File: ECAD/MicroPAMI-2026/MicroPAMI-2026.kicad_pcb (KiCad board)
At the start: 2 copper layers, 52 x 52 mm, 13 parts, among them J1 Conn_01x05, J2 Conn_01x05, SW3 SW_Push, U1 ATtiny3226-S, U2 ITR9608-F, U4 AMS1117-5.0, U5 ULN2803A

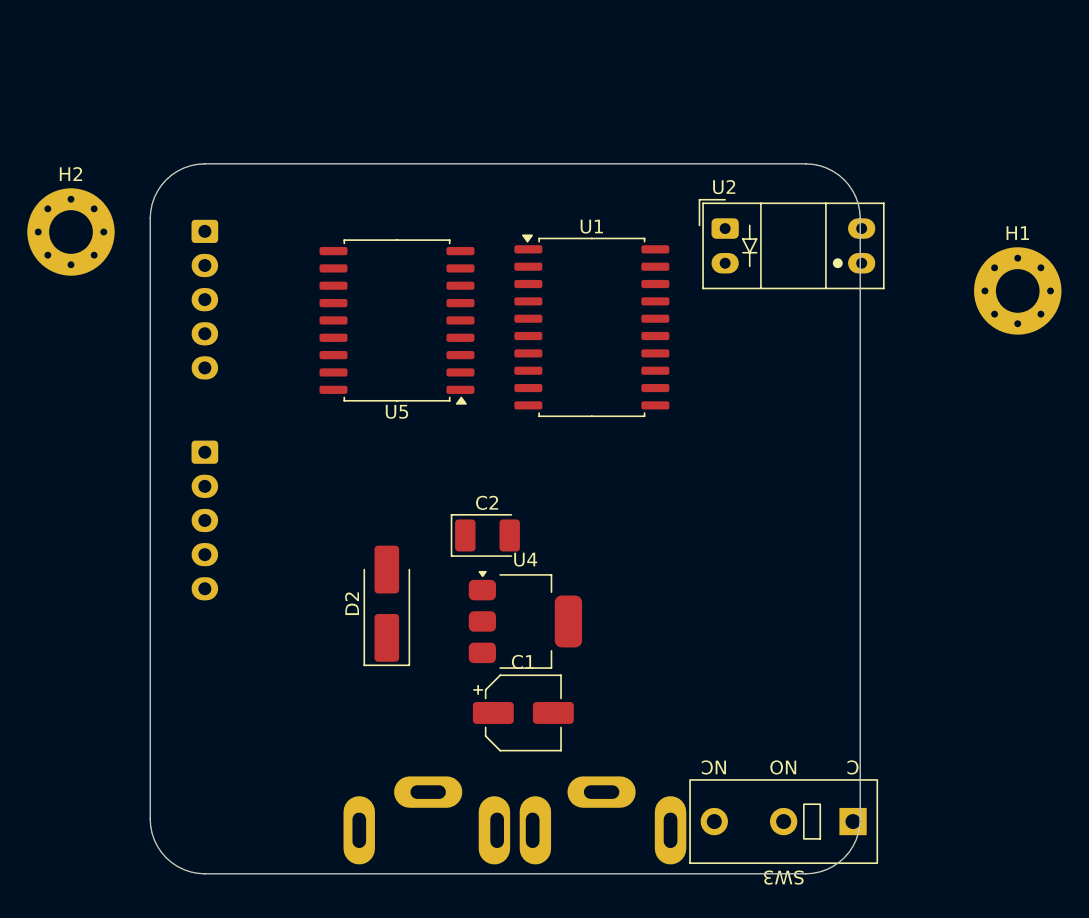
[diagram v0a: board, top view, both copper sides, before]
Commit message: Update PCB: add resistors, change net assignments
Added R3 and R8 SMD resistors to the PCB layout and updated net assignments for several signals, including connections for Tirette, LeftSensor, and others. Replaced unconnected net labels with specific net names for improved clarity. Updated backup files and made minor changes to project and cache files.
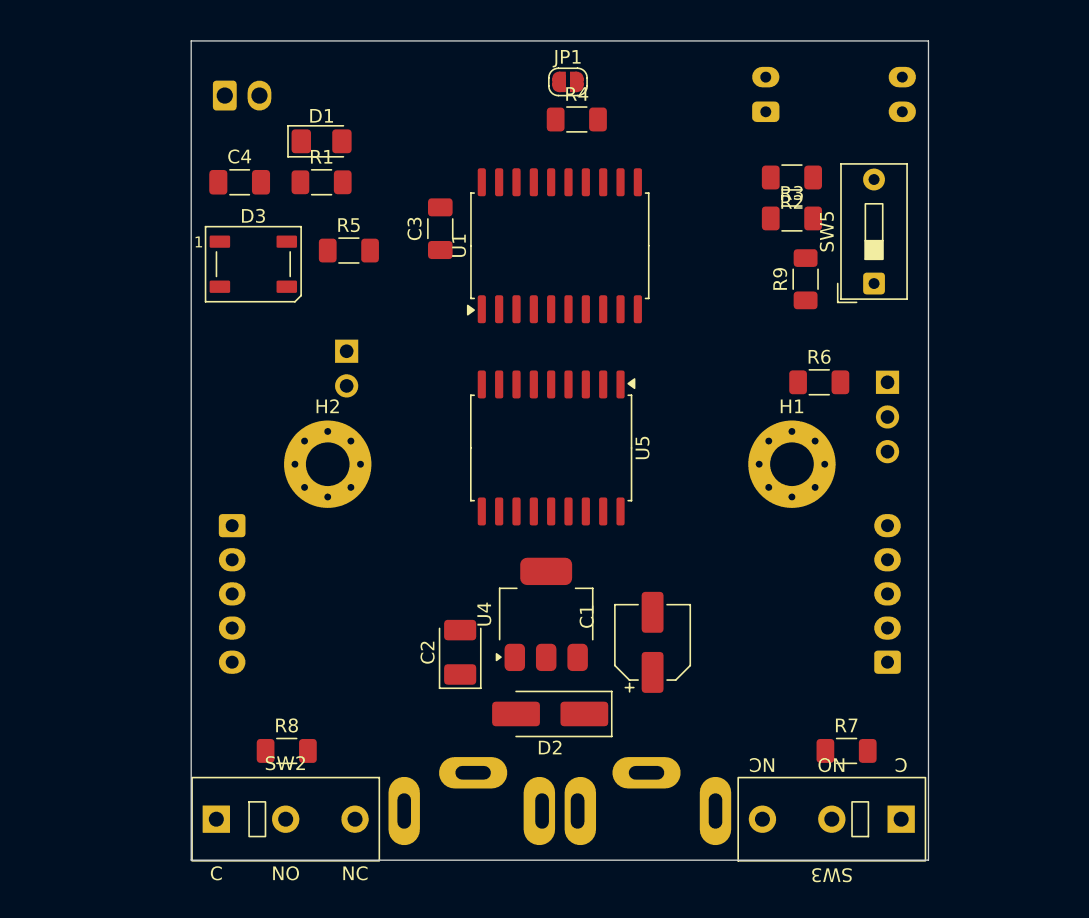
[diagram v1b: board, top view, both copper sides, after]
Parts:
- added C3: C_Small, Capacitor_SMD:C_1206_3216Metric_Pad1.33x1.80mm_HandSolder, F.Cu at (71.2, 70.8)
- added C4: C_Small, Capacitor_SMD:C_1206_3216Metric_Pad1.33x1.80mm_HandSolder, F.Cu at (56.5, 67.3)
- added D1: LED_Small, LED_SMD:LED_1206_3216Metric_Pad1.42x1.75mm_HandSolder, F.Cu at (62.5, 64.3)
- added D3: WS2812B, LED_SMD:LED_WS2812B_PLCC4_5.0x5.0mm_P3.2mm, F.Cu at (57.5, 73.3)
- added J3: MicroServo 2G, Connector_PinHeader_2.54mm:PinHeader_1x03_P2.54mm_Vertical, B.Cu at (104.0, 82.0)
- added J4: UPDI, Connector_PinHeader_2.54mm:PinHeader_1x02_P2.54mm_Horizontal, B.Cu at (64.4, 79.7)
- added JP1: Jumper_2_Small_Open, Jumper:SolderJumper-2_P1.3mm_Open_RoundedPad1.0x1.5mm, F.Cu at (80.6, 60.0)
- added R1: R_Small, Resistor_SMD:R_1206_3216Metric_Pad1.30x1.75mm_HandSolder, F.Cu at (62.5, 67.3)
- added R2: R_Small, Resistor_SMD:R_1206_3216Metric_Pad1.30x1.75mm_HandSolder, F.Cu at (97.0, 67.0)
- added R3: R_Small, Resistor_SMD:R_1206_3216Metric_Pad1.30x1.75mm_HandSolder, F.Cu at (97.0, 70.0)
- added R4: 4R7-470R, Resistor_SMD:R_1206_3216Metric_Pad1.30x1.75mm_HandSolder, F.Cu at (81.2, 62.8)
- added R5: 220, Resistor_SMD:R_1206_3216Metric_Pad1.30x1.75mm_HandSolder, F.Cu at (64.5, 72.3)
- added R6: 220, Resistor_SMD:R_1206_3216Metric_Pad1.30x1.75mm_HandSolder, F.Cu at (99.0, 82.0)
- added R7: 10k, Resistor_SMD:R_1206_3216Metric_Pad1.30x1.75mm_HandSolder, F.Cu at (101.0, 109.0)
- added R8: 10k, Resistor_SMD:R_1206_3216Metric_Pad1.30x1.75mm_HandSolder, F.Cu at (60.0, 109.0)
- added R9: 10k, Resistor_SMD:R_1206_3216Metric_Pad1.30x1.75mm_HandSolder, F.Cu at (98.0, 74.4)
- added SW1: SW_Push, Connector_Molex:Molex_KK-254_AE-6410-02A_1x02_P2.54mm_Vertical, B.Cu at (55.5, 61.0)
- added SW2: Left, Button_Switch_THT:SW_XKB_DM1-16UP-1, F.Cu at (54.8, 114.0)
- added SW5: SW_DIP_x01, Button_Switch_THT:SW_DIP_SPSTx01_Slide_9.78x4.72mm_W7.62mm_P2.54mm, F.Cu at (103.0, 74.8)
- BT1: value Battery_Cell -> 9V-Battery
- SW3: value SW_Push -> Right
- U2: moved to B.Cu
- moved J2 52.3 mm to (104.0, 102.5), turned to 90 degrees
- moved H2 25.4 mm to (63.0, 88.0)
- moved J1 21.6 mm to (56.0, 92.5)
- moved H1 20.8 mm to (97.0, 88.0)
- moved U5 14.7 mm to (79.4, 86.8), turned to -90 degrees
- moved D2 14.4 mm to (79.3, 106.3), turned to 180 degrees
- moved C1 10.8 mm to (86.8, 101.0), turned to 90 degrees
- moved U2 9.05 mm to (95.1, 62.2)
- moved C2 8.79 mm to (72.7, 101.8), turned to 90 degrees
- moved U1 6.42 mm to (80.0, 72.0), turned to 90 degrees
- moved BT1 3.58 mm to (80.0, 113.4)
- moved SW3 3.53 mm to (105.0, 114.0)
- moved U4 1.61 mm to (79.0, 99.0), turned to 90 degrees
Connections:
- BT1 pad 1: +9V -> Net-(BT1-+)
- SW3 pad 1: unconnected-(SW3-Pad1) -> RightSensor
- U1 pad 16: unconnected-(U1-~{RESET}/PA0-Pad16) -> /UPDI
- U2 pad 1: unconnected-(U2-Pad1) -> Net-(R2-Pad2)
- U2 pad 2: unconnected-(U2-Pad2) -> GND
- U2 pad 3: unconnected-(U2-Pad3) -> +5V
- U2 pad 4: unconnected-(U2-Pad4) -> Tirette
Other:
- board size 52 x 52 mm -> 54 x 60 mm

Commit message: Update battery position and change component orientation
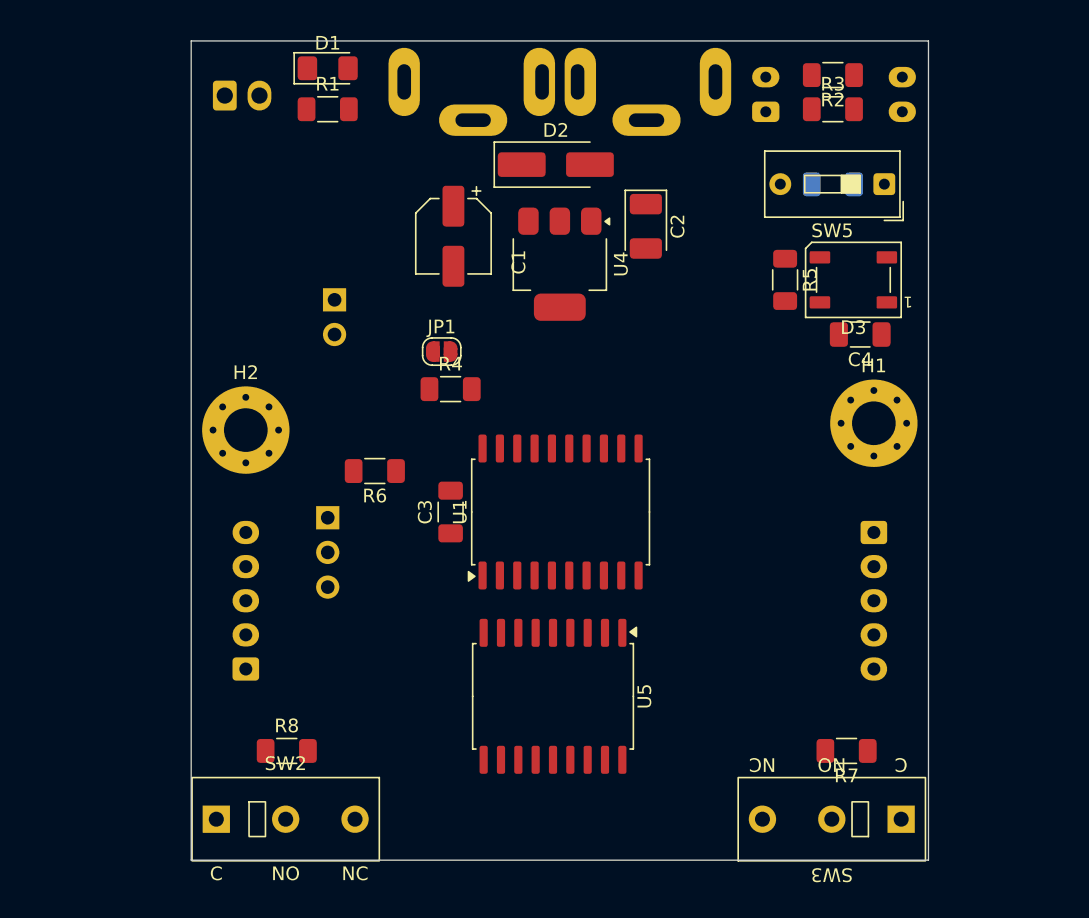
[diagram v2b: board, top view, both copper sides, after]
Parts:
- R9: moved to B.Cu
- moved BT1 53.4 mm to (80.0, 60.0), turned to 180 degrees
- moved C4 46.8 mm to (102.0, 78.5), turned to 180 degrees
- moved D3 44.0 mm to (101.5, 74.5), turned to 180 degrees
- moved J3 42.2 mm to (63.0, 91.9)
- moved D2 40.2 mm to (79.7, 66.1), turned to 0 degrees
- moved C2 34.0 mm to (86.3, 70.6), turned to -90 degrees
- moved R6 33.2 mm to (66.5, 88.5), turned to 180 degrees
- moved C1 33.1 mm to (72.2, 71.3), turned to -90 degrees
- moved R5 32.0 mm to (96.5, 74.5), turned to -90 degrees
- moved U4 25.7 mm to (80.0, 73.3), turned to -90 degrees
- moved JP1 21.8 mm to (71.3, 79.8)
- moved R4 21.8 mm to (72.0, 82.5)
- moved C3 20.8 mm to (72.0, 91.5)
- moved U1 19.5 mm to (80.1, 91.5)
- moved U5 18.2 mm to (79.5, 105.0)
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
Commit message: Board routing
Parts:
- removed J4: UPDI, Connector_PinHeader_2.54mm:PinHeader_1x02_P2.54mm_Horizontal
- added D5: SS14, Diode_SMD:D_SMA_Handsoldering, F.Cu at (70.5, 79.0)
- added J5: UPDI, Connector_PinHeader_2.54mm:PinHeader_1x03_P2.54mm_Vertical, B.Cu at (63.5, 86.1)
- moved R7 34.3 mm to (78.0, 83.5), turned to 90 degrees
- moved J3 34.0 mm to (96.5, 86.0), turned to 0 degrees
- moved R8 29.8 mm to (75.5, 83.5), turned to 90 degrees
- moved R6 25.6 mm to (92.0, 87.0), turned to 0 degrees
- moved D1 9.79 mm to (58.5, 67.7), turned to 90 degrees
- moved JP1 9.77 mm to (67.0, 88.5), turned to 180 degrees
- moved SW1 8.54 mm to (64.0, 61.0), turned to 180 degrees
- moved SW5 7.26 mm to (96.5, 68.0), turned to 0 degrees
- moved R4 6.10 mm to (67.0, 86.0), turned to 180 degrees
- moved R1 4.53 mm to (58.5, 62.5), turned to -90 degrees
- moved C3 4.32 mm to (72.8, 95.8)
- moved C2 4.21 mm to (88.6, 74.1)
- moved J1 4.00 mm to (57.0, 107.0)
- moved J2 4.00 mm to (103.0, 97.0)
- moved D2 3.98 mm to (82.8, 68.5)
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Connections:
- net Net-(BT1-+) renamed +BATT
- U1 pad 12: unconnected-(U1-PC0-Pad12) -> SERVO
- U1 pad 13: unconnected-(U1-PC1-Pad13) -> TEAM_COLOR
- U1 pad 14: unconnected-(U1-PC2-Pad14) -> ColorSelector
- U1 pad 15: unconnected-(U1-PC3-Pad15) -> Tirette
- U1 pad 18: unconnected-(U1-PA2-Pad18) -> RightSensor
- U1 pad 19: unconnected-(U1-PA3-Pad19) -> LeftSensor
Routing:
- net +9V: track 0.00 -> 150.9 mm, vias 0 -> 1
- net +5V: track 0.00 -> 123.4 mm, vias 0 -> 3
- net RightSensor: track 0.00 -> 53.9 mm, vias 0 -> 1
- net LeftSensor: track 0.00 -> 48.3 mm, vias 0 -> 1
- net Tirette: track 0.00 -> 44.9 mm, vias 0 -> 2
- net ColorSelector: track 0.00 -> 30.3 mm, vias 0 -> 1
- net Net-(J1-Pin_4): track 0.00 -> 30.0 mm
- net Net-(J2-Pin_1): track 0.00 -> 28.5 mm
- net Net-(J1-Pin_3): track 0.00 -> 26.8 mm
- net Net-(J2-Pin_2): track 0.00 -> 26.3 mm
- net Net-(J1-Pin_2): track 0.00 -> 25.4 mm
- net Net-(J2-Pin_3): track 0.00 -> 24.9 mm
- net Net-(J1-Pin_1): track 0.00 -> 24.6 mm
- net Net-(J2-Pin_4): track 0.00 -> 24.1 mm
- net TEAM_COLOR: track 0.00 -> 22.5 mm, vias 0 -> 2
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- added copper zone on F.Cu, net +9V
- added copper zone on F.Cu, net +BATT
- added copper zone on B.Cu, net GND
- added copper zone on F.Cu, net GND
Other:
- outline, holes or cut-outs redrawn

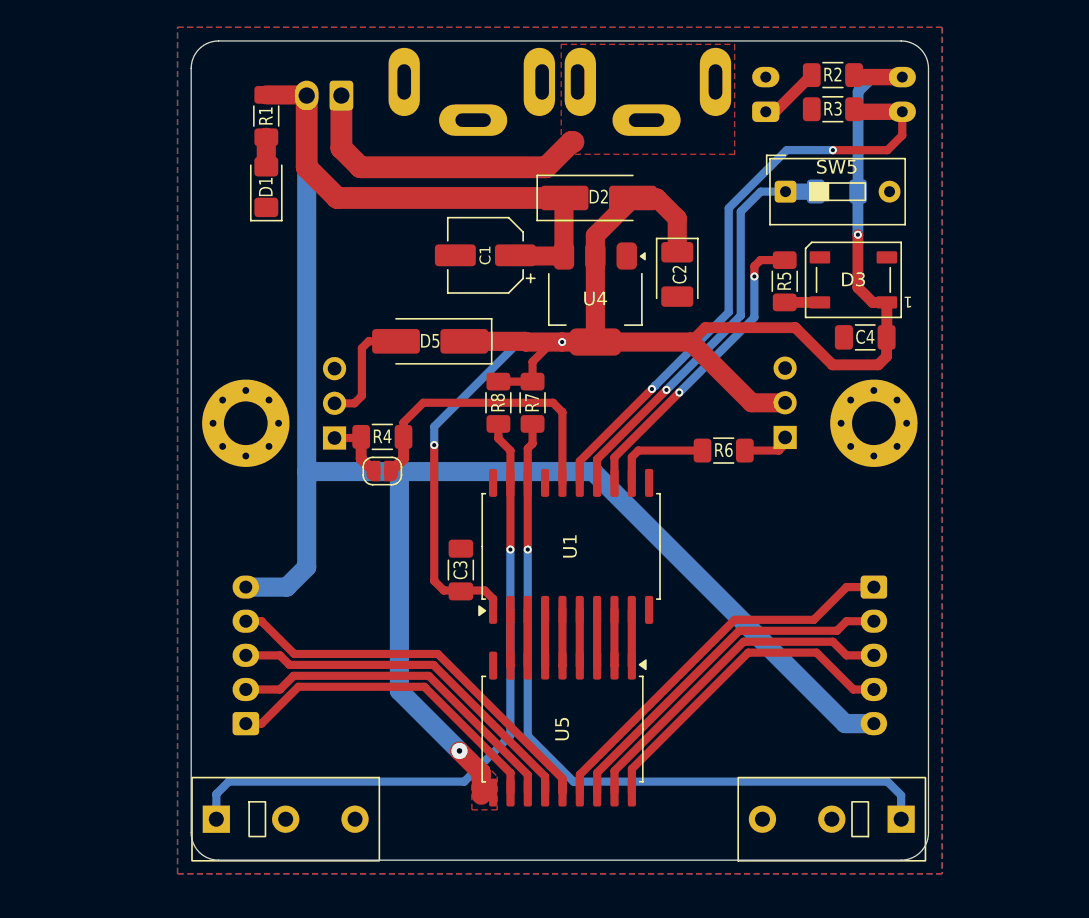
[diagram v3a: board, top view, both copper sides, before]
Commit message: update BAU - add oled
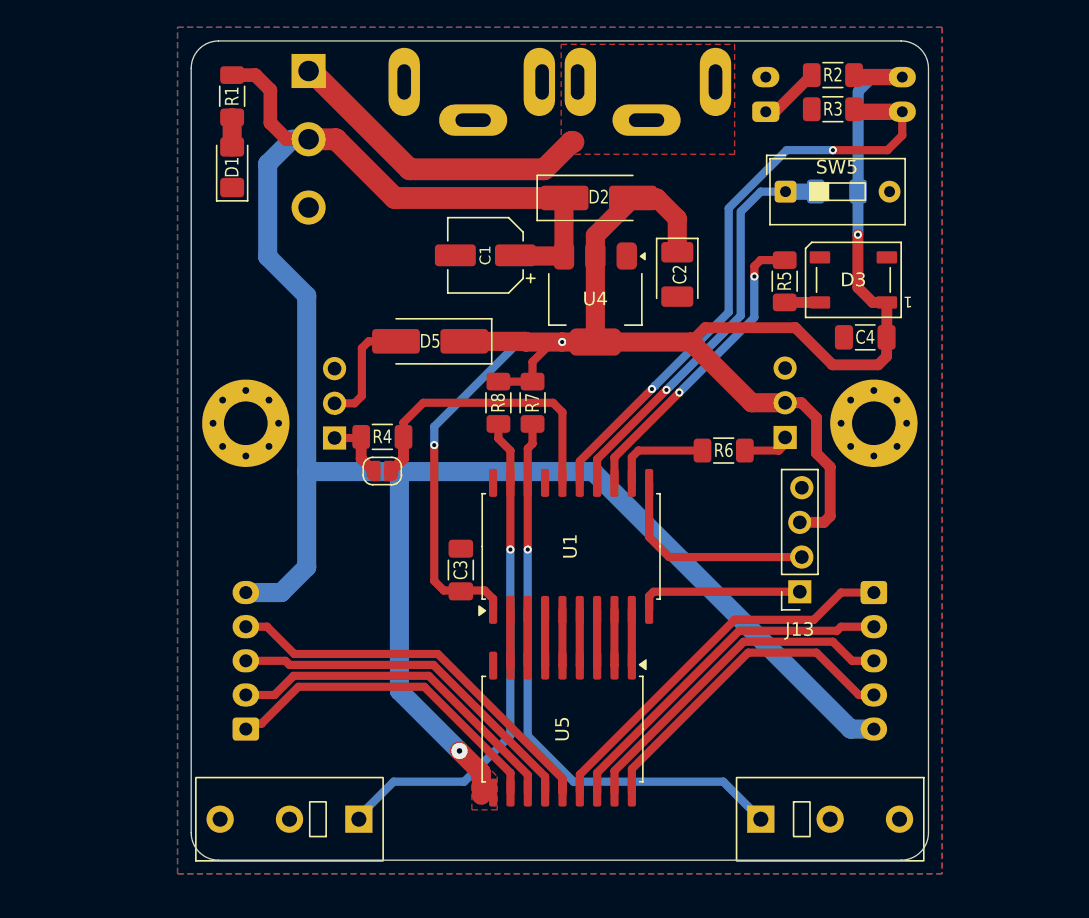
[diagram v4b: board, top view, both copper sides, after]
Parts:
- removed SW1: SW_Push, Connector_Molex:Molex_KK-254_AE-6410-02A_1x02_P2.54mm_Vertical
- added J13: OLED, Connector_PinSocket_2.54mm:PinSocket_1x04_P2.54mm_Vertical, F.Cu at (97.6, 97.3)
- added SW4: SW_SPDT, Switch:SK-12D10 1P2T, B.Cu at (61.6, 64.2)
- moved SW2 10.4 mm to (65.3, 114.0), turned to 180 degrees
- moved SW3 10.3 mm to (94.7, 114.0), turned to 0 degrees
- moved D1 2.89 mm to (56.0, 66.2)
- moved R1 2.89 mm to (56.0, 61.0)
- moved J1 0.40 mm to (57.0, 107.4)
- moved J2 0.40 mm to (103.0, 97.4)
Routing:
- net SCL: track 0.00 -> 15.6 mm
- net +5V: track 123.4 -> 136.2 mm
- net SDA: track 0.00 -> 12.2 mm
- net LeftSensor: track 48.3 -> 36.9 mm
- net RightSensor: track 53.9 -> 42.6 mm
- net +9V: track 150.9 -> 152.6 mm
- net +BATT: track 22.2 -> 23.2 mm

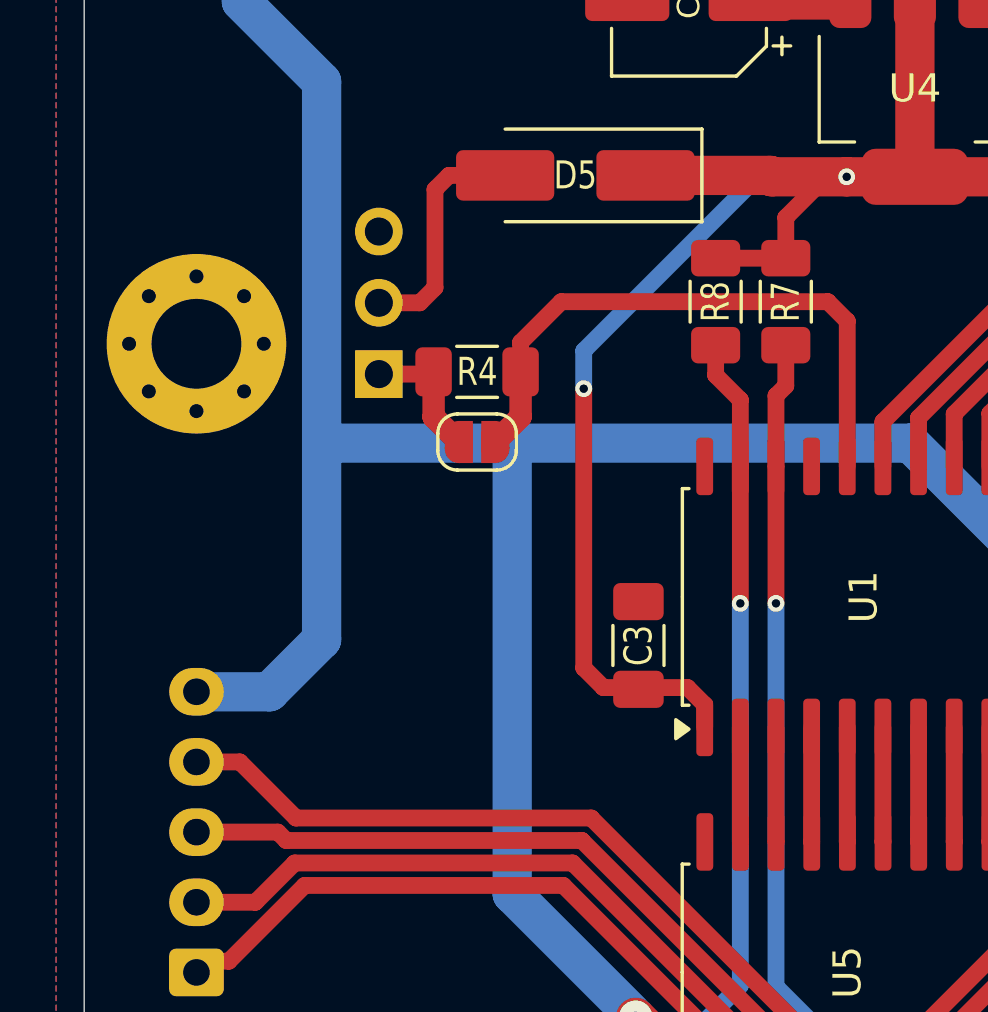
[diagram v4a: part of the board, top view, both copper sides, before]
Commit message: add a robot selector jumper
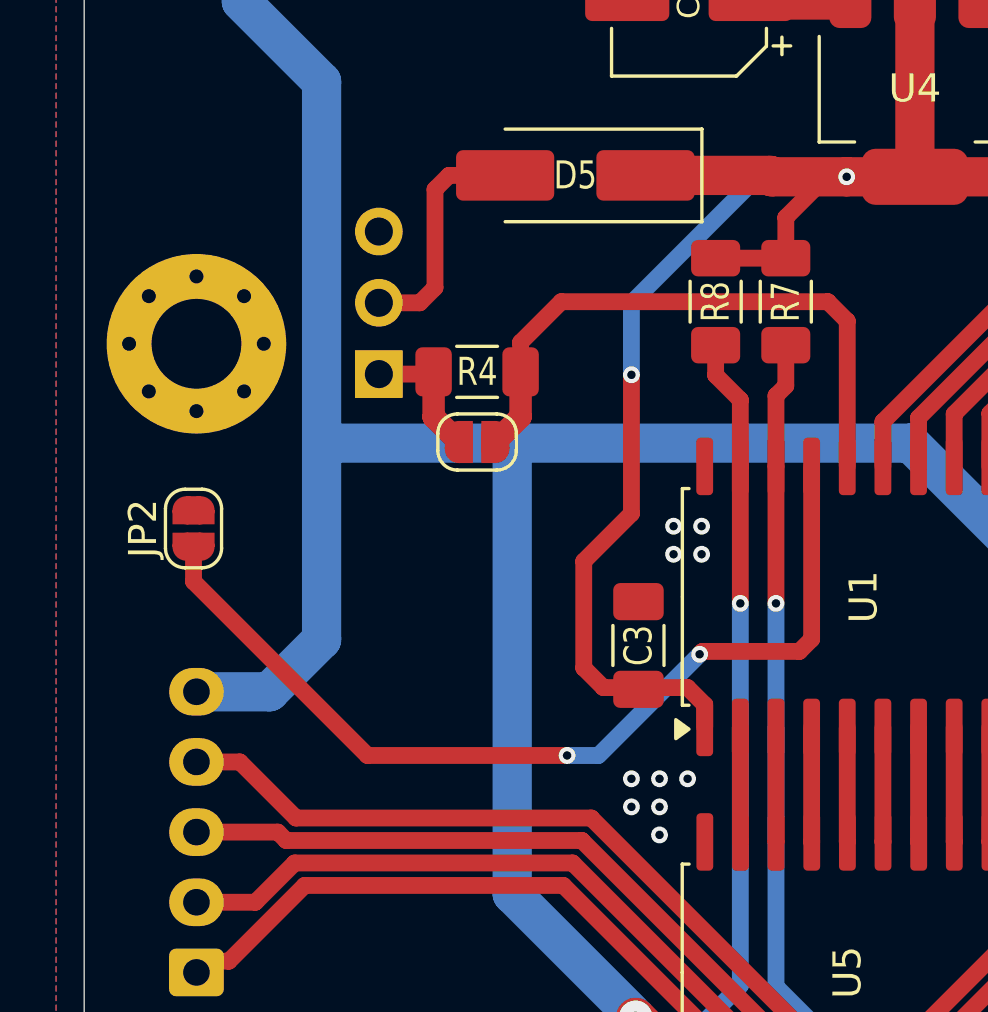
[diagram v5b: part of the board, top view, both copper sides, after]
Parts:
- added JP2: Robot_selector, Jumper:SolderJumper-2_P1.3mm_Open_RoundedPad1.0x1.5mm, F.Cu at (56.9, 91.6)
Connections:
- U1 pad 17: unconnected-(U1-PA1-Pad17) -> Net-(JP2-A)
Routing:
- net Net-(JP2-A): track 0.00 -> 33.7 mm, vias 0 -> 2
- net GND: vias 0 -> 10
